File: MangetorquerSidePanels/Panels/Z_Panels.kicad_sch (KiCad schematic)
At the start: 57 parts, among them J1 SMA Connector Male, J2 Through_Hole_1, Q1 BSS138DWQ-7, Q2 MBT2222ADW1T1, Q3 BSS138DWQ-7, Q4 MBT2222ADW1T1, U1 DRV8830DGQ, U2 BD60GC0WEFJ, U3 HHM1589D1, U4 OPT3001

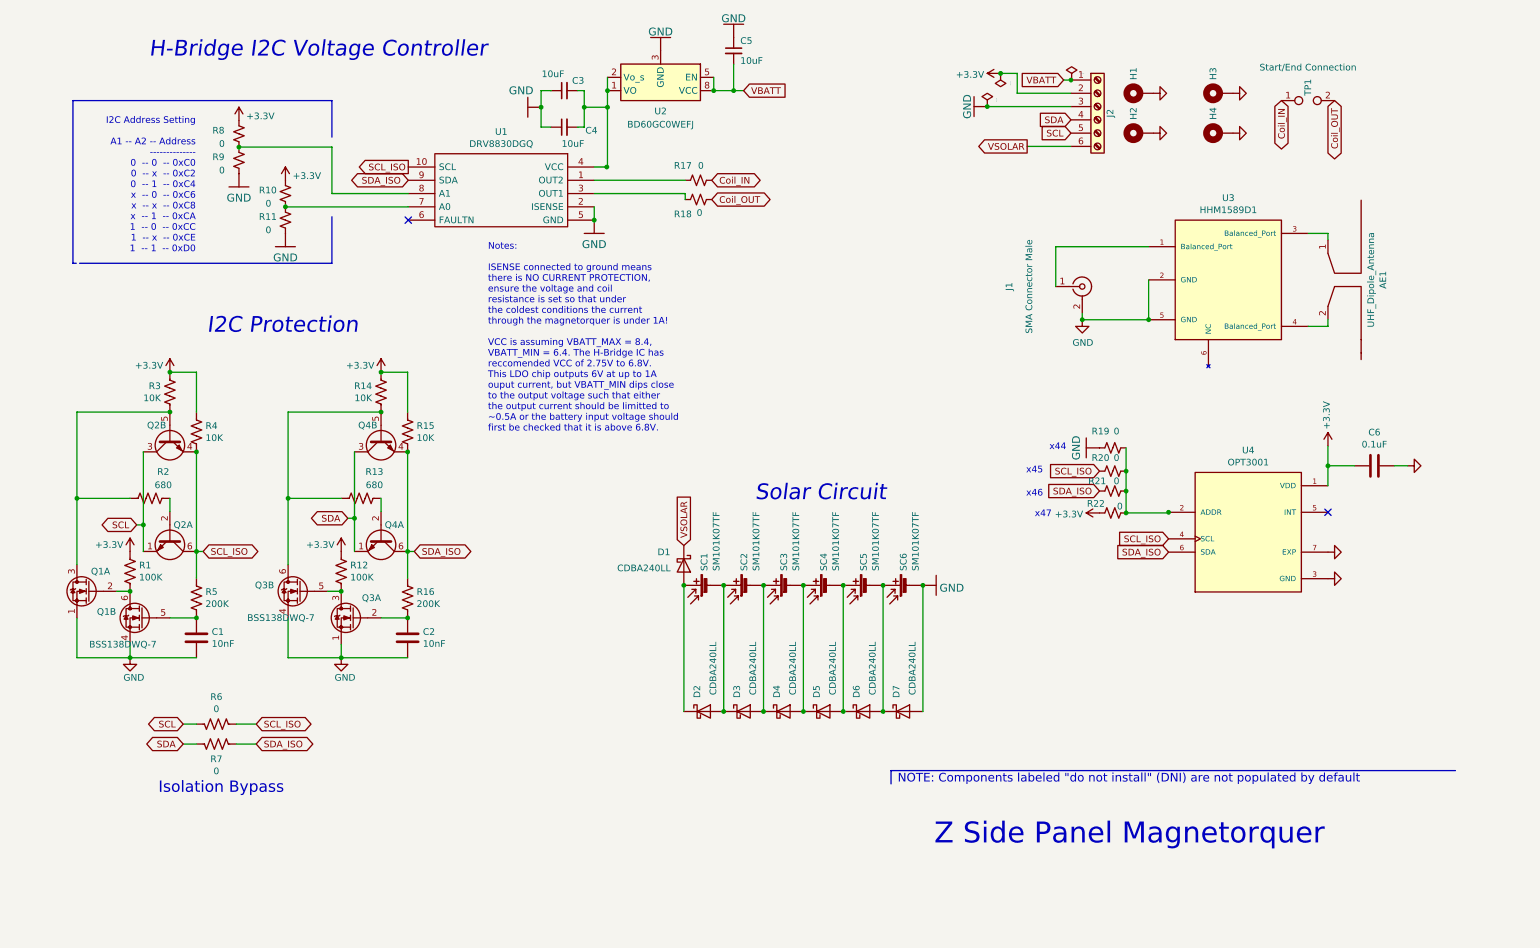
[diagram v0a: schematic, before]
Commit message: Final flight side panels w/ magnetorquers finished, note final board thickness of 0.031'' and updated copper weight of 0.5oz for internal layers
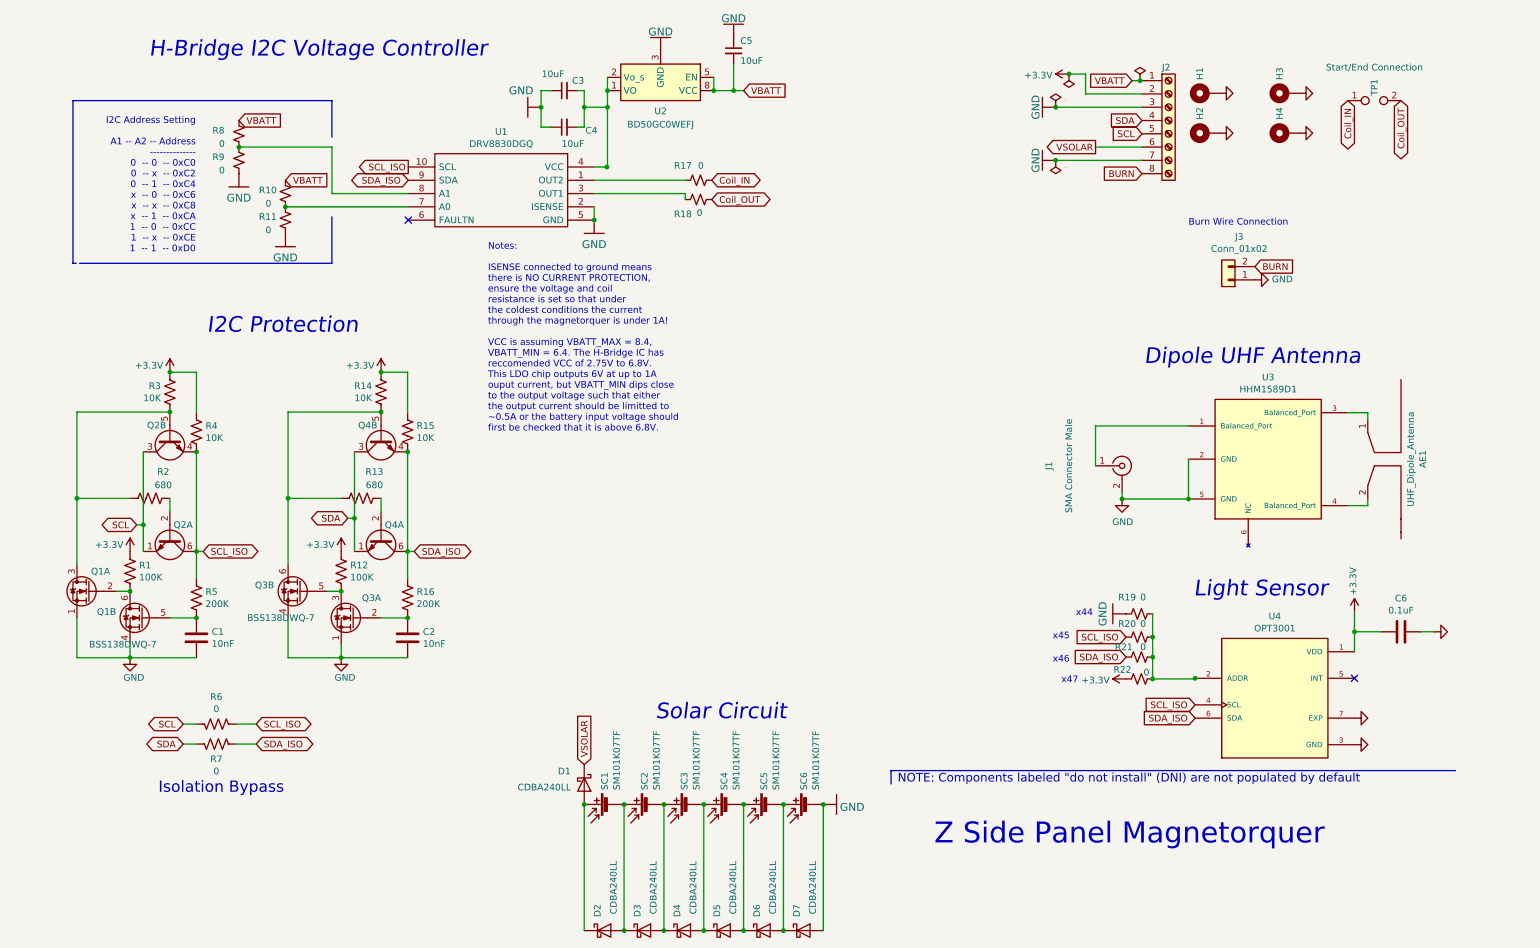
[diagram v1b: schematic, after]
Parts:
- removed J2: Through_Hole_1, Connector_PinHeader_2.54mm:PinHeader_1x06_P2.54mm_Vertical, symbol Connector:Screw_Terminal_01x06
- added J2: Screw_Terminal_01x08, Connector_PinHeader_2.54mm:PinHeader_1x08_P2.54mm_Vertical, symbol Connector:Screw_Terminal_01x08
- added J3: Conn_01x02, panels:Burn_Wire_Connection, symbol Connector_Generic:Conn_01x02
- U2: value BD60GC0WEFJ -> BD50GC0WEFJ
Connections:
- net +3V3: now also J2.2 (Pin_2); no longer R10.1, R8.1
- net GND: now also J2.3 (Pin_3), J2.7 (Pin_7), J3.1 (Pin_1)
- net SCL: now also J2.5 (Pin_5)
- net SDA: now also J2.4 (Pin_4)
- net VBATT: now also R10.1, R8.1, J2.1 (Pin_1)
- net VSOLAR: now also J2.6 (Pin_6)
- new net BURN: J2.8 (Pin_8), J3.2 (Pin_2)
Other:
- note added: "Burn Wire Connection"
- note added: "Dipole UHF Antenna"
- note added: "Light Sensor"
- moved on the sheet: AE1, C6, D1, D2, D3, D4, D5, D6, D7, H1, H2, H3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

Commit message: added magnetorquers
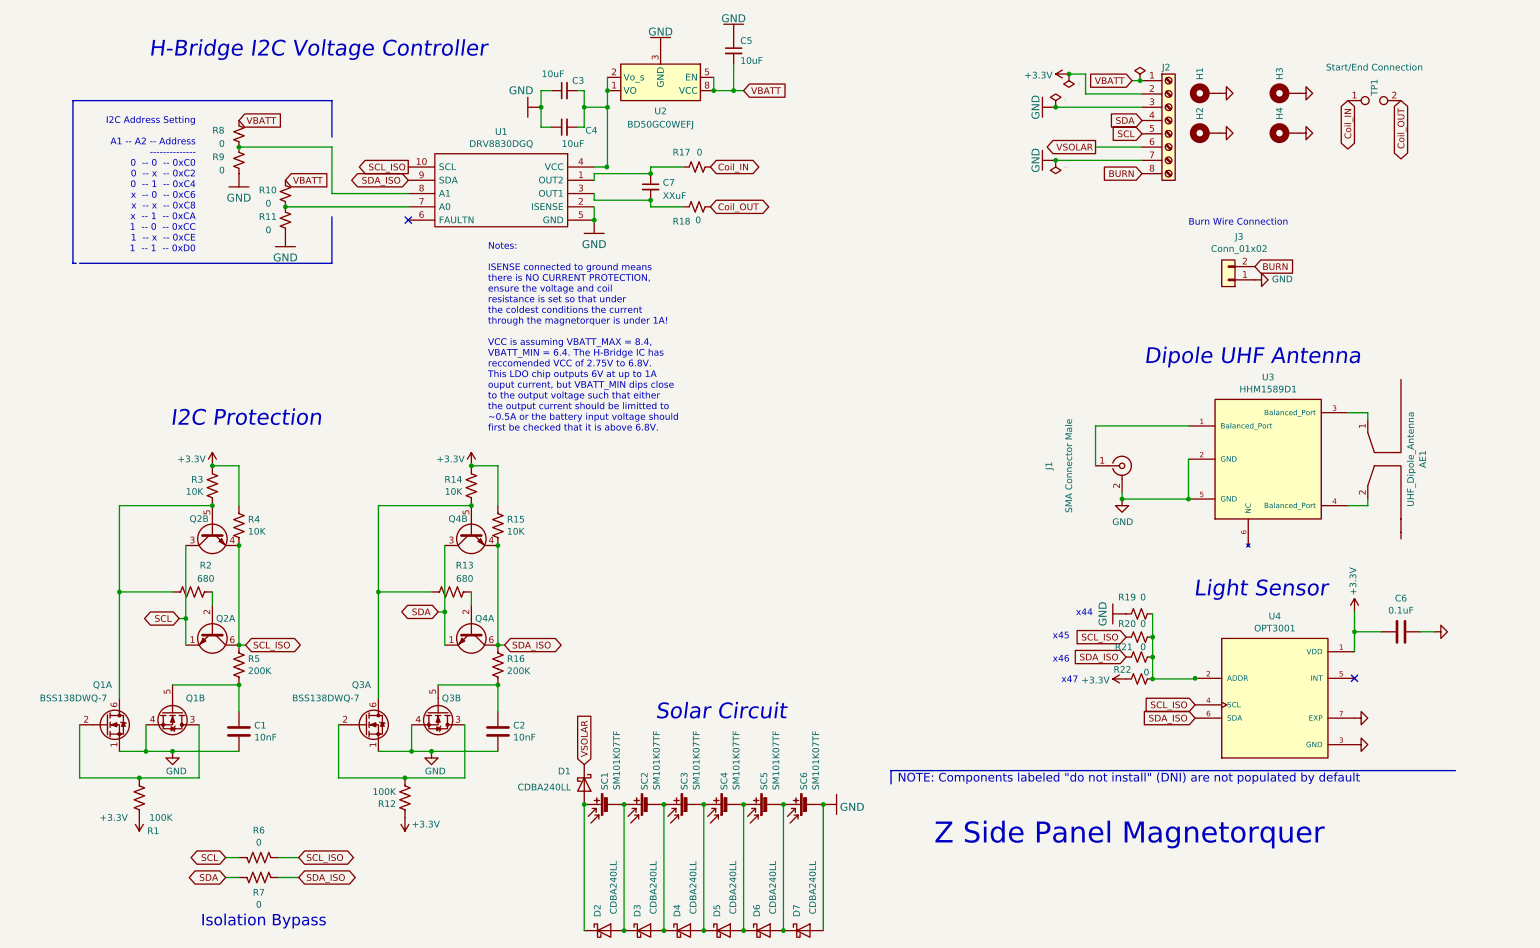
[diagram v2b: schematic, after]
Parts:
- removed Q1, Q3: BSS138DWQ-7, panels:BSS138DWQ-7, symbol xpanel-rescue:BSS138DWQ-7-symbols
- added C7: XXuF, Capacitor_SMD:C_1210_3225Metric, symbol Device:C_Small
- added Q1, Q3: BSS138DWQ-7, panels:BSS138DWQ-7, symbol Sapling_Side_Panels:BSS138DWQ-7
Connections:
- net GND: now also Q1.1 (S2), Q1.4 (S1), Q3.1 (S2), Q3.4 (S1)
- net at Q4.5 (B2), R13.2, R14.2: now also Q3.6 (D1)
- net at C2.1, R16.1: now also Q3.5 (G1)
- net at R1.1: now also Q1.2 (G2), Q1.3 (D2)
- net at Q2.5 (B2), R2.1, R3.2: now also Q1.6 (D1)
- net at C1.1, R5.1: now also Q1.5 (G1)
- net at R12.1: now also Q3.2 (G2), Q3.3 (D2)
- net at R17.1, U1.1 (OUT2): now also C7.1
- net at R18.1, U1.3 (OUT1): now also C7.2
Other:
- moved on the sheet: R17, R18
